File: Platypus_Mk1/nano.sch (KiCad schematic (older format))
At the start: 24 parts, among them J10 ICSP, J9 UJ2-BH-1-TH, K1 SW_RESET, U2 INTERFACE-CH340T_SSOP20_, U3 MCU-ATMEGA328P-AU_TQFP32_, Y1 12MHz, Y2 16MHZ

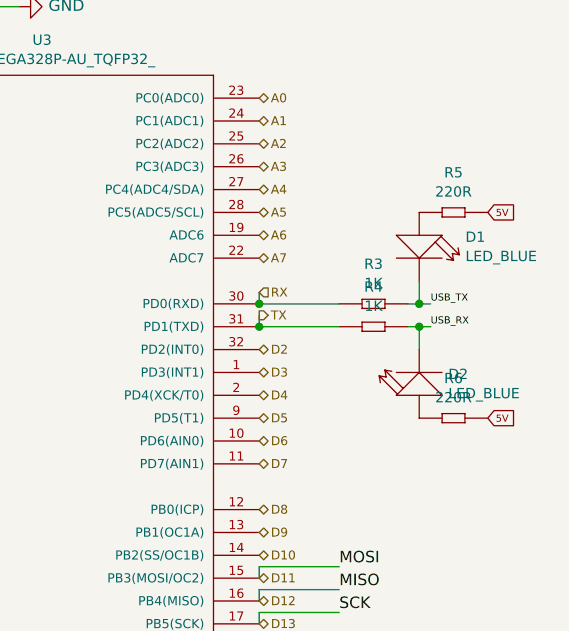
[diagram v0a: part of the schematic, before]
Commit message: Change RX/TX LEDs. Add new laser conn
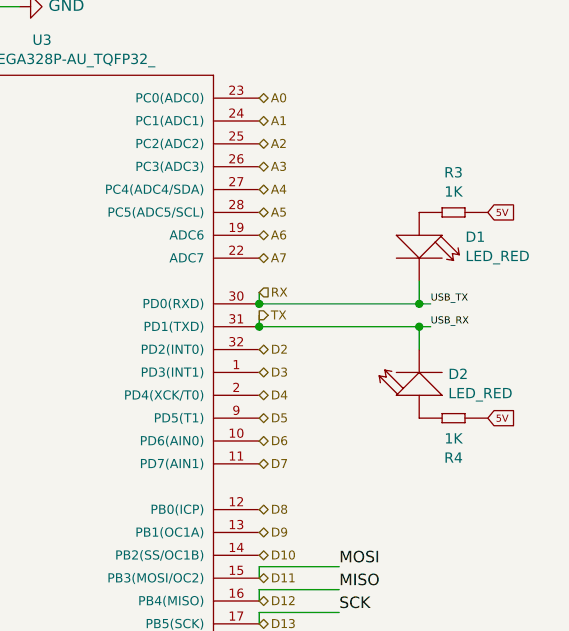
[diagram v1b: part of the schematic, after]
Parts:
- removed R5, R6: 220R, OPL_Resistor:R0603, symbol OPL_Resistor:SMD-RES-220R-5%-1_10W_0603_
- D1, D2: value LED_BLUE -> LED_RED; MPN 19-217-BHC-ZL1M2RY-3T -> 19-217-R6C-AL1M2VY-3T; SKU 304090045 -> 304090042
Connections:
- net 5V: now also R3.2, R4.1
- net RX: now also D1.2 (-), U2.3 (TXD); no longer R3.1
- net TX: now also D2.2 (-), U2.4 (RXD); no longer R4.1
- net at D1.1 (+): now also R3.1
- net at D2.1 (+): now also R4.2
- removed net USB_RX: D2.2 (-), R4.2, U2.4 (RXD)
- removed net USB_TX: D1.2 (-), R3.2, U2.3 (TXD)
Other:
- moved on the sheet: R3, R4
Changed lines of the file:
@@
 	0    1    1    0
 $EndComp
-Wire Wire Line
-	10050 3050 10100 3050
 Text Label 10150 3150 0    31   ~ 0
 USB_RX
-Wire Wire Line
-	10050 3150 10100 3150
 Wire Wire Line
 	7350 2150 7450 2150
@@
 Text GLabel 5550 1750 2    31   Input ~ 0
 5V
-Wire Wire Line
-	10100 2950 10100 3050
-Connection ~ 10100 3050
-Wire Wire Line
-	10100 3050 10150 3050
 $Comp
 L OPL_Resistor:SMD-RES-1K-1%-1_10W_0603_ R3
 U 1 1 5D4DC1D9
-P 9900 3050
+P 10250 2650
 AR Path="/5D499913/5D4DC1D9" Ref="R3"  Part="1"
 AR Path="/5D4AF8B7/5D4DC1D9" Ref="R?"  Part="1"
-F 0 "R3" H 9900 3224 45  0000 C CNN
-F 1 "1K" H 9900 3140 45  0000 C CNN
-F 2 "OPL_Resistor:R0603" H 9900 3050 40  0001 C CNN
-F 3 "" H 9900 3050 40  0001 C CNN
-F 4 "RC0603FR-071KL" H 9930 3200 20  0001 C CNN "MPN"
-F 5 "301010298" H 9930 3200 20  0001 C CNN "SKU"
-	1    9900 3050
+F 0 "R3" H 10250 2824 45  0000 C CNN
+F 1 "1K" H 10250 2740 45  0000 C CNN
+F 2 "OPL_Resistor:R0603" H 10250 2650 40  0001 C CNN
+F 3 "" H 10250 2650 40  0001 C CNN
+F 4 "RC0603FR-071KL" H 10280 2800 20  0001 C CNN "MPN"
+F 5 "301010298" H 10280 2800 20  0001 C CNN "SKU"
+	1    10250 2650
 	1    0    0    -1
 $EndComp
@@
 AR Path="/5D4AF8B7/5D4DFDA7" Ref="D?"  Part="1"
 F 0 "D1" V 10058 3002 45  0000 L CNN
-F 1 "LED_BLUE" V 10142 3002 45  0000 L CNN
+F 1 "LED_RED" V 10142 3002 45  0000 L CNN
 F 2 "OPL_Optoelectronics:LED-0603" H 10100 2800 50  0001 C CNN
 F 3 "" H 10100 2800 50  0001 C CNN
-F 4 "19-217-BHC-ZL1M2RY-3T" H 10130 2950 20  0001 C CNN "MPN"
-F 5 "304090045" H 10130 2950 20  0001 C CNN "SKU"
+F 4 "19-217-R6C-AL1M2VY-3T" H 10130 2950 20  0001 C CNN "MPN"
+F 5 "304090042" H 10130 2950 20  0001 C CNN "SKU"
 	1    10100 2800
 	0    1    1    0
@@
 AR Path="/5D4AF8B7/5D4E0FF9" Ref="D?"  Part="1"
 F 0 "D2" V 10142 3273 45  0000 R CNN
-F 1 "LED_BLUE" V 10058 3273 45  0000 R CNN
+F 1 "LED_RED" V 10058 3273 45  0000 R CNN
 F 2 "OPL_Optoelectronics:LED-0603" H 10100 3400 50  0001 C CNN
 F 3 "" H 10100 3400 50  0001 C CNN
-F 4 "19-217-BHC-ZL1M2RY-3T" H 10130 3550 20  0001 C CNN "MPN"
-F 5 "304090045" H 10130 3550 20  0001 C CNN "SKU"
+F 4 "19-217-R6C-AL1M2VY-3T" H 10130 3550 20  0001 C CNN "MPN"
+F 5 "304090042" H 10130 3550 20  0001 C CNN "SKU"
 	1    10100 3400
 	0    -1   -1   0
-$EndComp
-$Comp
-L OPL_Resistor:SMD-RES-220R-5%-1_10W_0603_ R5
-U 1 1 5D4E2240
-P 10250 2650
-AR Path="/5D499913/5D4E2240" Ref="R5"  Part="1"
-AR Path="/5D4AF8B7/5D4E2240" Ref="R?"  Part="1"
-F 0 "R5" H 10250 2824 45  0000 C CNN
-F 1 "220R" H 10250 2740 45  0000 C CNN
-F 2 "OPL_Resistor:R0603" H 10250 2736 40  0001 C CNN
-F 3 "" H 10250 2650 40  0001 C CNN
-F 4 "RC0603JR-07220RL" H 10280 2800 20  0001 C CNN "MPN"
-F 5 "301010163" H 10280 2800 20  0001 C CNN "SKU"
-	1    10250 2650
-	1    0    0    -1
 $EndComp
 Wire Wire Line
@@
 L OPL_Resistor:SMD-RES-1K-1%-1_10W_0603_ R4
 U 1 1 5D4F4CF3
-P 9900 3150
+P 10250 3550
 AR Path="/5D499913/5D4F4CF3" Ref="R4"  Part="1"
 AR Path="/5D4AF8B7/5D4F4CF3" Ref="R?"  Part="1"
-F 0 "R4" H 9900 3324 45  0000 C CNN
-F 1 "1K" H 9900 3240 45  0000 C CNN
-F 2 "OPL_Resistor:R0603" H 9900 3150 40  0001 C CNN
-F 3 "" H 9900 3150 40  0001 C CNN
-F 4 "RC0603FR-071KL" H 9930 3300 20  0001 C CNN "MPN"
-F 5 "301010298" H 9930 3300 20  0001 C CNN "SKU"
-	1    9900 3150
-	1    0    0    -1
-$EndComp
-$Comp
-L OPL_Resistor:SMD-RES-220R-5%-1_10W_0603_ R6
-U 1 1 5D4E2F3F
-P 10250 3550
-AR Path="/5D499913/5D4E2F3F" Ref="R6"  Part="1"
-AR Path="/5D4AF8B7/5D4E2F3F" Ref="R?"  Part="1"
-F 0 "R6" H 10250 3724 45  0000 C CNN
-F 1 "220R" H 10250 3640 45  0000 C CNN
-F 2 "OPL_Resistor:R0603" H 10250 3636 40  0001 C CNN
+F 0 "R4" H 10250 3724 45  0000 C CNN
+F 1 "1K" H 10250 3640 45  0000 C CNN
+F 2 "OPL_Resistor:R0603" H 10250 3550 40  0001 C CNN
 F 3 "" H 10250 3550 40  0001 C CNN
-F 4 "RC0603JR-07220RL" H 10280 3700 20  0001 C CNN "MPN"
-F 5 "301010163" H 10280 3700 20  0001 C CNN "SKU"
+F 4 "RC0603FR-071KL" H 10280 3700 20  0001 C CNN "MPN"
+F 5 "301010298" H 10280 3700 20  0001 C CNN "SKU"
 	1    10250 3550
-	1    0    0    -1
+	-1   0    0    1
 $EndComp
 $Comp
@@
 	9400 3000 9400 3050
 Connection ~ 9400 3050
-Wire Wire Line
-	9400 3050 9750 3050
-Wire Wire Line
-	9400 3150 9750 3150
 Text HLabel 6900 1400 2    50   Input ~ 0
 RST
@@
 Wire Wire Line
 	6750 3650 7150 3650
+Wire Wire Line
+	10100 3050 10150 3050
+Wire Wire Line
+	10100 2950 10100 3050
+Connection ~ 10100 3050
+Wire Wire Line
+	9400 3050 10100 3050
+Wire Wire Line
+	9400 3150 10100 3150
 $EndSCHEMATC
